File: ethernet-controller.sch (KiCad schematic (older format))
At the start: 39 parts, among them J1 5-2337992-8, U1 RTL8111H, Y1 ABM8G-25.000MHZ-18-D2Y-T

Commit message: Loclib
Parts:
- TP10, TP3, TP4, TP5, TP6, TP7, TP8, TP9: footprint antmicro-footprints:Testpoint_smd_0_75mm -> sa800u-baseboard-hw-footprints:Testpoint_smd_0_75mm; symbol antmicroTestPoints:TP_SMD_0_75MM -> sa800u-baseboard-hw:TP_SMD_0_75MM
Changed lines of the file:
@@
 PCIE1_RX_C_P
 $Comp
-L antmicroTestPoints:TP_SMD_0_75MM TP3
+L sa800u-baseboard-hw:TP_SMD_0_75MM TP3
 U 1 1 624394EB
 P 4500 3000
 F 0 "TP3" H 4500 2905 50  0000 C CNN
 F 1 "TP_SMD_0_75MM" H 4500 2900 50  0001 C CNN
-F 2 "antmicro-footprints:Testpoint_smd_0_75mm" H 4700 3200 60  0001 L CNN
+F 2 "sa800u-baseboard-hw-footprints:Testpoint_smd_0_75mm" H 4700 3200 60  0001 L CNN
 F 3 "" H 4700 3300 60  0001 L CNN
 	1    4500 3000
@@
 $EndComp
 $Comp
-L antmicroTestPoints:TP_SMD_0_75MM TP9
+L sa800u-baseboard-hw:TP_SMD_0_75MM TP9
 U 1 1 6243B4E7
 P 7850 2975
 F 0 "TP9" H 7850 2880 50  0000 C CNN
 F 1 "TP_SMD_0_75MM" H 7850 2875 50  0001 C CNN
-F 2 "antmicro-footprints:Testpoint_smd_0_75mm" H 8050 3175 60  0001 L CNN
+F 2 "sa800u-baseboard-hw-footprints:Testpoint_smd_0_75mm" H 8050 3175 60  0001 L CNN
 F 3 "" H 8050 3275 60  0001 L CNN
 	1    7850 2975
@@
 $EndComp
 $Comp
-L antmicroTestPoints:TP_SMD_0_75MM TP4
+L sa800u-baseboard-hw:TP_SMD_0_75MM TP4
 U 1 1 62446EB7
 P 6100 4775
 F 0 "TP4" H 6100 4680 50  0000 C CNN
 F 1 "TP_SMD_0_75MM" H 6100 4675 50  0001 C CNN
-F 2 "antmicro-footprints:Testpoint_smd_0_75mm" H 6300 4975 60  0001 L CNN
+F 2 "sa800u-baseboard-hw-footprints:Testpoint_smd_0_75mm" H 6300 4975 60  0001 L CNN
 F 3 "" H 6300 5075 60  0001 L CNN
 	1    6100 4775
@@
 $EndComp
 $Comp
-L antmicroTestPoints:TP_SMD_0_75MM TP6
+L sa800u-baseboard-hw:TP_SMD_0_75MM TP6
 U 1 1 6244F4AE
 P 6375 4775
 F 0 "TP6" H 6375 4680 50  0000 C CNN
 F 1 "TP_SMD_0_75MM" H 6375 4675 50  0001 C CNN
-F 2 "antmicro-footprints:Testpoint_smd_0_75mm" H 6575 4975 60  0001 L CNN
+F 2 "sa800u-baseboard-hw-footprints:Testpoint_smd_0_75mm" H 6575 4975 60  0001 L CNN
 F 3 "" H 6575 5075 60  0001 L CNN
 	1    6375 4775
@@
 $EndComp
 $Comp
-L antmicroTestPoints:TP_SMD_0_75MM TP7
+L sa800u-baseboard-hw:TP_SMD_0_75MM TP7
 U 1 1 62457423
 P 6625 4775
 F 0 "TP7" H 6625 4680 50  0000 C CNN
 F 1 "TP_SMD_0_75MM" H 6625 4675 50  0001 C CNN
-F 2 "antmicro-footprints:Testpoint_smd_0_75mm" H 6825 4975 60  0001 L CNN
+F 2 "sa800u-baseboard-hw-footprints:Testpoint_smd_0_75mm" H 6825 4975 60  0001 L CNN
 F 3 "" H 6825 5075 60  0001 L CNN
 	1    6625 4775
@@
 	6625 5125 6950 5125
 $Comp
-L antmicroTestPoints:TP_SMD_0_75MM TP5
+L sa800u-baseboard-hw:TP_SMD_0_75MM TP5
 U 1 1 6247C502
 P 6325 6125
 F 0 "TP5" H 6200 6100 50  0000 C CNN
 F 1 "TP_SMD_0_75MM" H 6325 6025 50  0001 C CNN
-F 2 "antmicro-footprints:Testpoint_smd_0_75mm" H 6525 6325 60  0001 L CNN
+F 2 "sa800u-baseboard-hw-footprints:Testpoint_smd_0_75mm" H 6525 6325 60  0001 L CNN
 F 3 "" H 6525 6425 60  0001 L CNN
 	1    6325 6125
@@
 	6325 6225 6950 6225
 $Comp
-L antmicroTestPoints:TP_SMD_0_75MM TP8
+L sa800u-baseboard-hw:TP_SMD_0_75MM TP8
 U 1 1 6249C84E
 P 6800 6425
 F 0 "TP8" V 6705 6472 50  0000 C CNN
 F 1 "TP_SMD_0_75MM" H 6800 6325 50  0001 C CNN
-F 2 "antmicro-footprints:Testpoint_smd_0_75mm" H 7000 6625 60  0001 L CNN
+F 2 "sa800u-baseboard-hw-footprints:Testpoint_smd_0_75mm" H 7000 6625 60  0001 L CNN
 F 3 "" H 7000 6725 60  0001 L CNN
 	1    6800 6425
@@
 Connection ~ 6900 6425
 $Comp
-L antmicroTestPoints:TP_SMD_0_75MM TP10
+L sa800u-baseboard-hw:TP_SMD_0_75MM TP10
 U 1 1 624AD4ED
 P 8500 2975
 F 0 "TP10" H 8500 2880 50  0000 C CNN
 F 1 "TP_SMD_0_75MM" H 8500 2875 50  0001 C CNN
-F 2 "antmicro-footprints:Testpoint_smd_0_75mm" H 8700 3175 60  0001 L CNN
+F 2 "sa800u-baseboard-hw-footprints:Testpoint_smd_0_75mm" H 8700 3175 60  0001 L CNN
 F 3 "" H 8700 3275 60  0001 L CNN
 	1    8500 2975

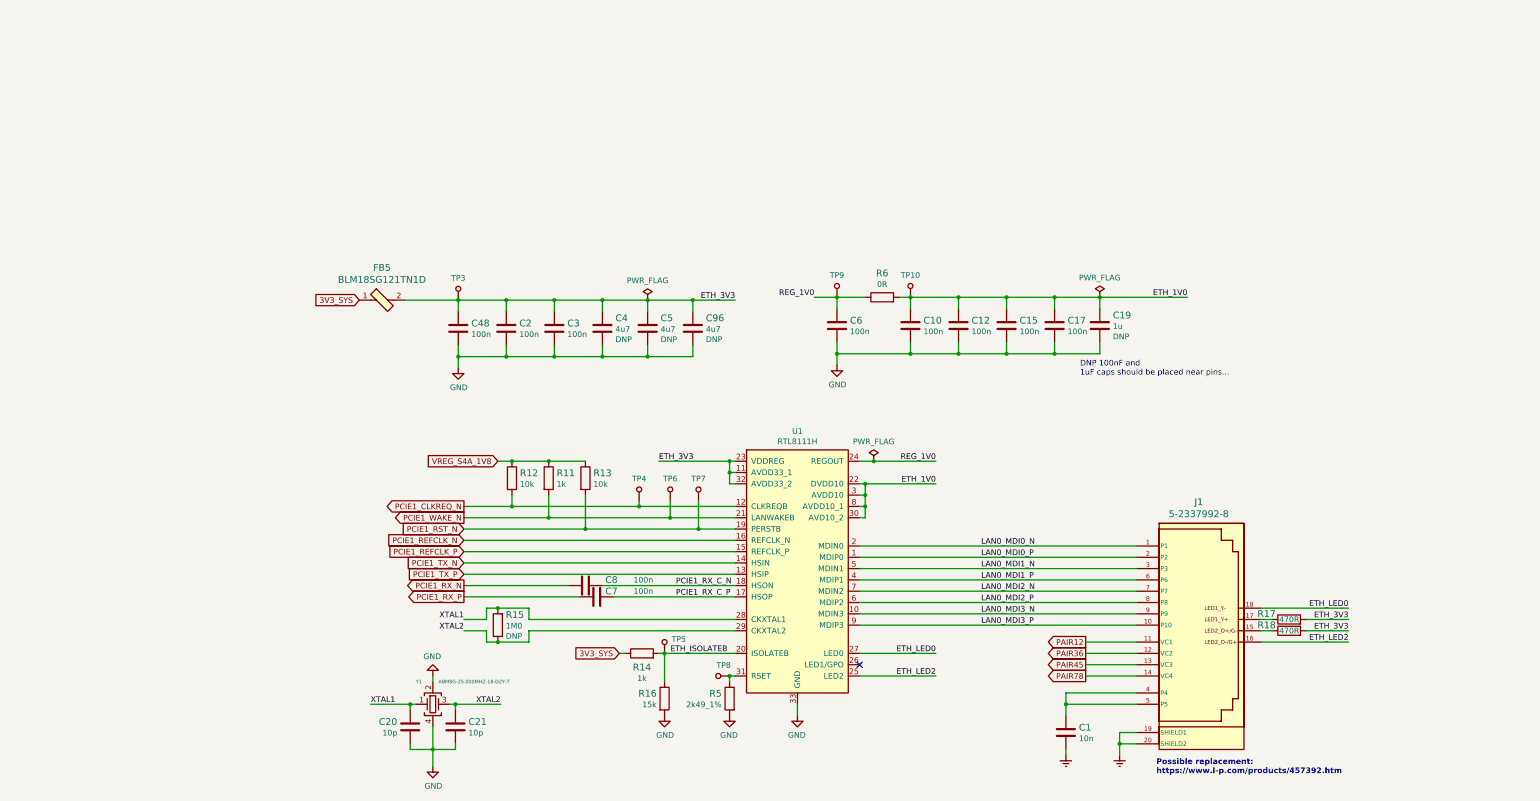
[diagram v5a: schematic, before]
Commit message: Reorganize schematics, add descriptions in top left corner
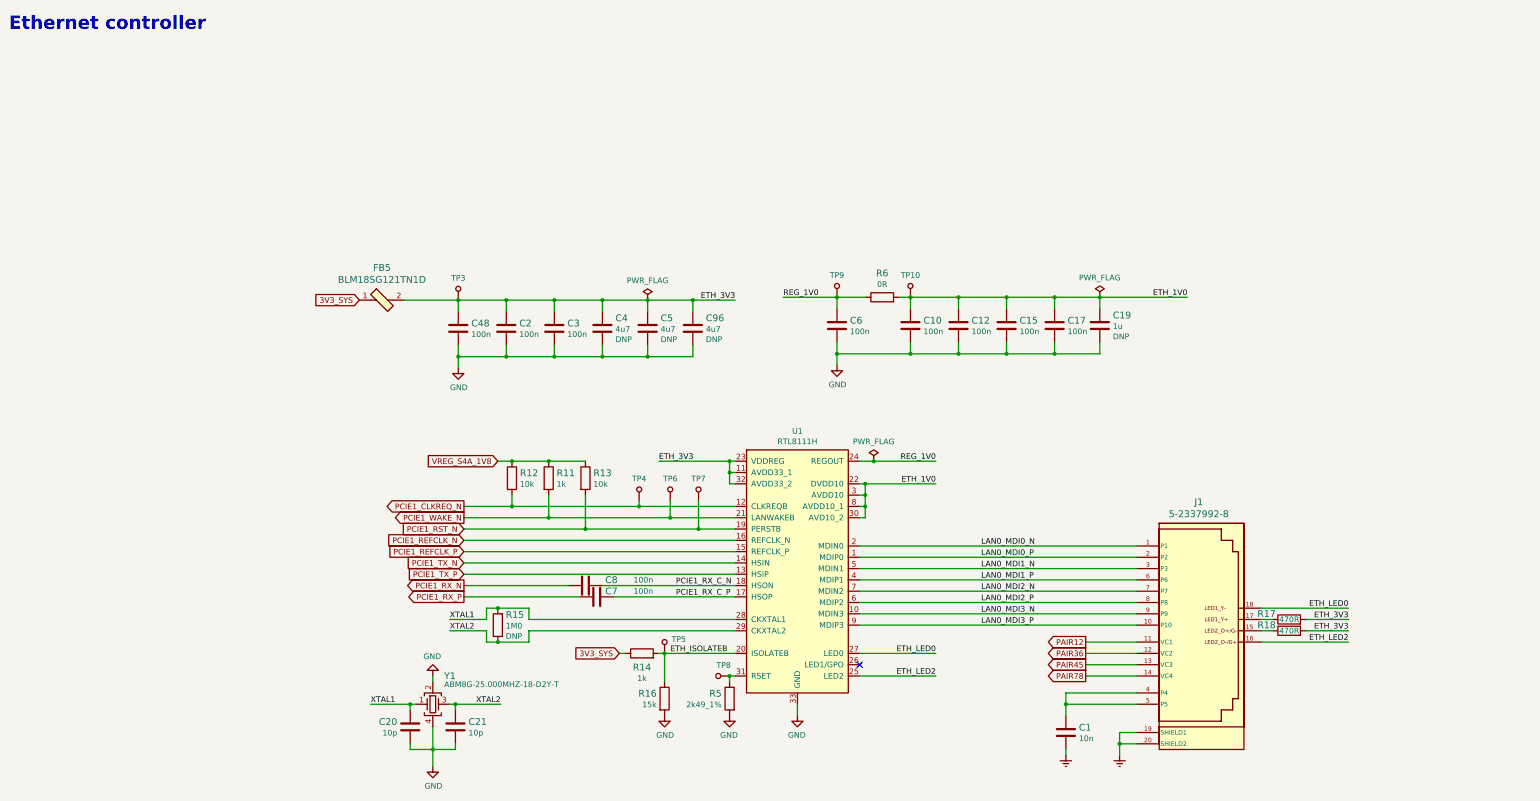
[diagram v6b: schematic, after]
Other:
- note added: "Ethernet controller"
- note removed: "DNP 100nF and \n1uF caps should be placed near pins..."
- note removed: "Possible replacement:\nhttps://www.l-p.com/products/457392.htm"
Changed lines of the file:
@@
 U 1 1 6246C7D0
 P 4275 6675
-F 0 "Y1" H 4125 6875 31  0000 L CNN
-F 1 "ABM8G-25.000MHZ-18-D2Y-T" H 4325 6875 31  0000 L CNN
+F 0 "Y1" H 4375 6925 60  0000 L CNN
+F 1 "ABM8G-25.000MHZ-18-D2Y-T" H 4375 6850 50  0000 L CNN
 F 2 "sa800u-baseboard-hw-footprints:KX-7" H 6375 6675 50  0001 C CNN
 F 3 "" H 6475 6775 50  0001 C CNN
@@
 Wire Wire Line
 	10050 6425 10500 6425
-Text Notes 10675 7300 0    50   ~ 10
-Possible replacement:\nhttps://www.l-p.com/products/457392.htm
 Text GLabel 3625 3100 0    50   Input ~ 0
 3V3_SYS
@@
 Connection ~ 9350 3575
 Connection ~ 9350 3075
-Text Notes 10000 3775 0    50   ~ 0
-DNP 100nF and \n1uF caps should be placed near pins...
 $Comp
 L sa800u-baseboard-hw:C_100n_0402 C48
@@
 ETH_1V0
 Wire Wire Line
-	7650 3075 7850 3075
-Text Label 7650 3075 2    50   ~ 0
+	7375 3075 7850 3075
+Text Label 7375 3075 0    50   ~ 0
 REG_1V0
 $Comp
@@
 Text Label 8725 6225 2    50   ~ 0
 ETH_LED0
-Text Label 4550 5925 2    50   ~ 0
+Text Label 4425 5925 0    50   ~ 0
 XTAL1
-Text Label 4550 6025 2    50   ~ 0
+Text Label 4425 6025 0    50   ~ 0
 XTAL2
 Text GLabel 4550 5525 0    50   Input ~ 0
@@
 Connection ~ 4850 5825
 Wire Wire Line
-	4550 5925 4750 5925
+	4425 5925 4750 5925
 Wire Wire Line
 	4750 5925 4750 5825
 Wire Wire Line
-	4550 6025 4750 6025
+	4425 6025 4750 6025
 Wire Wire Line
 	4750 6025 4750 6125
@@
 Wire Wire Line
 	11600 6125 12375 6125
+Text Notes 525  725  0    118  ~ 24
+Ethernet controller
 $EndSCHEMATC

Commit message: Clear annotation and annotate
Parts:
- renumbered C20 to C1, C96 to C10, C6 to C11, C10 to C12, C12 to C13, C15 to C14, C17 to C15, C1 to C16, C19 to C17, C21 to C2, C48 to C3, C2 to C4, C3 to C5, C8 to C6, C4 to C8, C5 to C9, FB5 to FB1, R16 to R10, R5 to R11, R6 to R12, R17 to R13, R18 to R14, R15 to R5, R12 to R6, R11 to R7, R13 to R8, R14 to R9, TP3 to TP1, TP4 to TP2, TP5 to TP3, TP6 to TP4, TP7 to TP5, TP8 to TP6, TP9 to TP7, TP10 to TP8
